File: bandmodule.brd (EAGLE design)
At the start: 100 x 80 mm, 15 parts

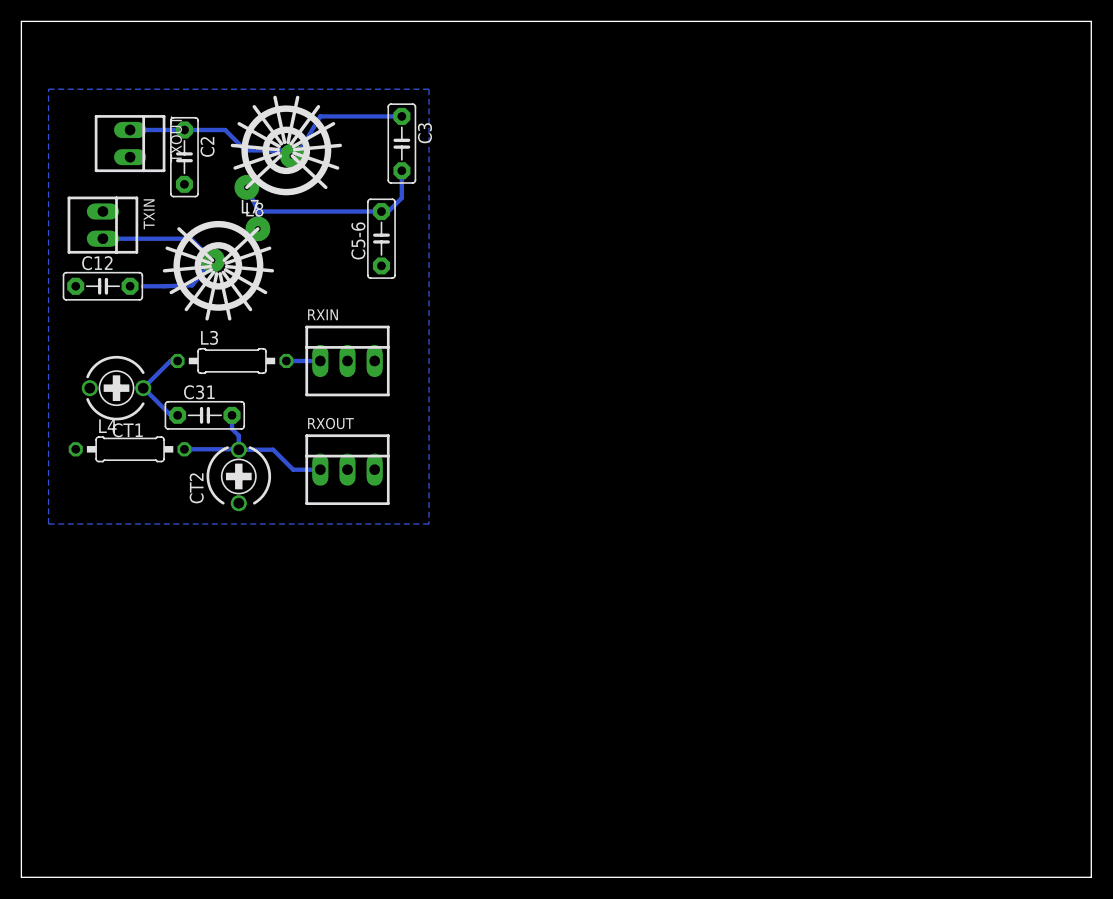
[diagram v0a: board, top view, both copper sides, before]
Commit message: Make board smaller
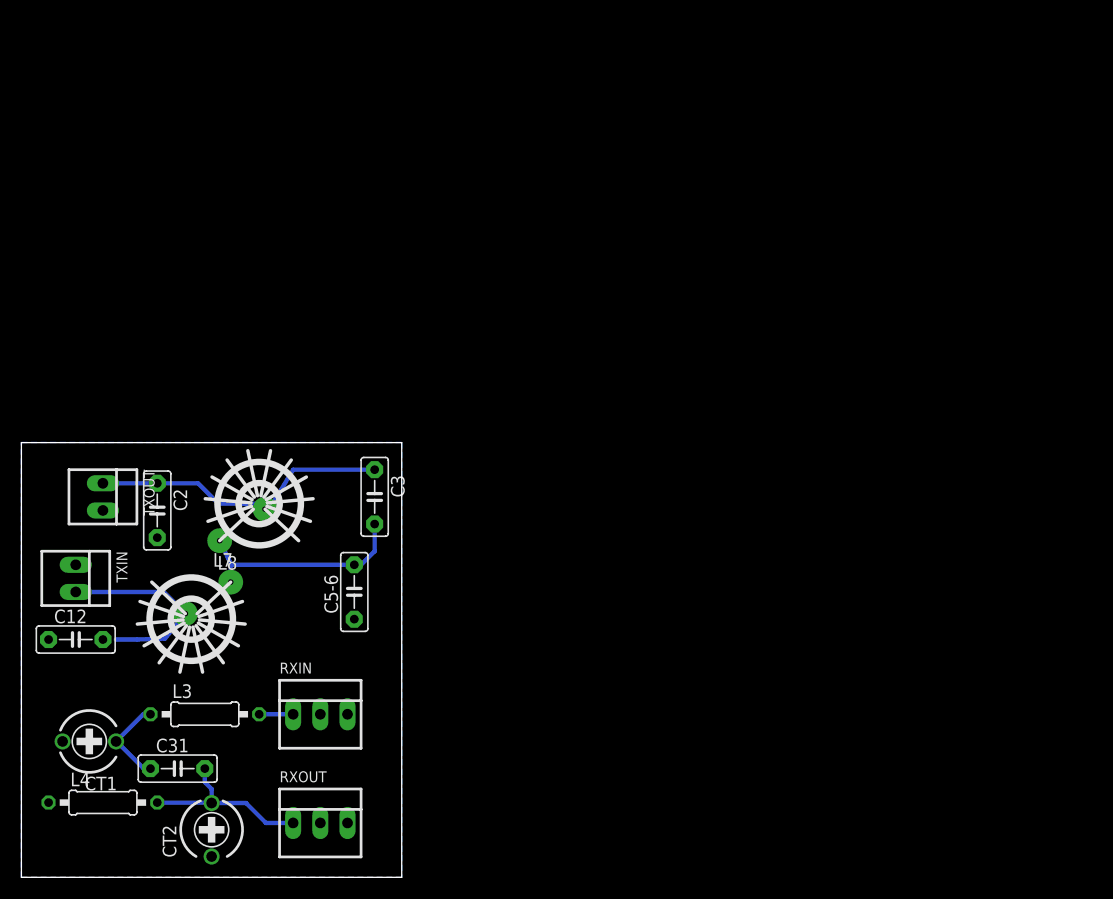
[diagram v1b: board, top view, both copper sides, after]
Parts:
- moved C2 33.1 mm to (12.7, 34.3)
- moved CT2 33.1 mm to (17.8, 4.45)
- moved L4 33.1 mm to (7.62, 6.99)
- moved RXOUT 33.1 mm to (27.9, 5.08)
- moved C12 33.1 mm to (5.08, 22.2)
- moved C3 33.1 mm to (33.0, 35.6)
- moved C31 33.1 mm to (14.6, 10.2)
- moved C5-6 33.1 mm to (31.1, 26.7)
- moved CT1 33.1 mm to (6.35, 12.7)
- moved L3 33.1 mm to (17.1, 15.2)
- moved L7 33.1 mm to (15.9, 24.1)
- moved L8 33.1 mm to (22.2, 34.9)
- moved RXIN 33.1 mm to (27.9, 15.2)
- moved TXIN 33.1 mm to (5.08, 27.9)
- moved TXOUT 33.1 mm to (7.62, 35.6)
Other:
- board size 100 x 80 mm -> 35.5 x 40.6 mm

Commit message: Readme, made more space for toroids
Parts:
- moved L7 1.42 mm to (17.1, 24.8)
- moved C3 1.14 mm to (32.1, 36.2)
- moved C5-6 1.14 mm to (30.2, 27.3)
- moved L8 0.71 mm to (21.9, 35.6), turned to 90 degrees
- moved C12 0.71 mm to (5.40, 22.9)
- moved CT1 0.64 mm to (6.35, 13.3)
- moved C31 0.63 mm to (14.6, 10.8)
- moved CT2 0.63 mm to (17.8, 5.08)
- moved L3 0.63 mm to (17.1, 15.9)
- moved L4 0.63 mm to (7.62, 7.62)
- moved RXIN 0.63 mm to (27.9, 15.9)
- moved RXOUT 0.63 mm to (27.9, 5.71)
- moved C2 0.63 mm to (12.7, 34.9)
- moved TXIN 0.63 mm to (5.08, 28.6)
- moved TXOUT 0.63 mm to (7.62, 36.2)
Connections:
- net GND: now also C12.1; no longer C12.2
- net N$6: now also C12.2; no longer C12.1
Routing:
- net N$8: track 33.7 -> 26.0 mm
- net N$5: track 20.7 -> 17.0 mm
- net N$6: track 18.7 -> 15.4 mm
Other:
- board size 35.5 x 40.6 mm -> 35.5 x 41.3 mm

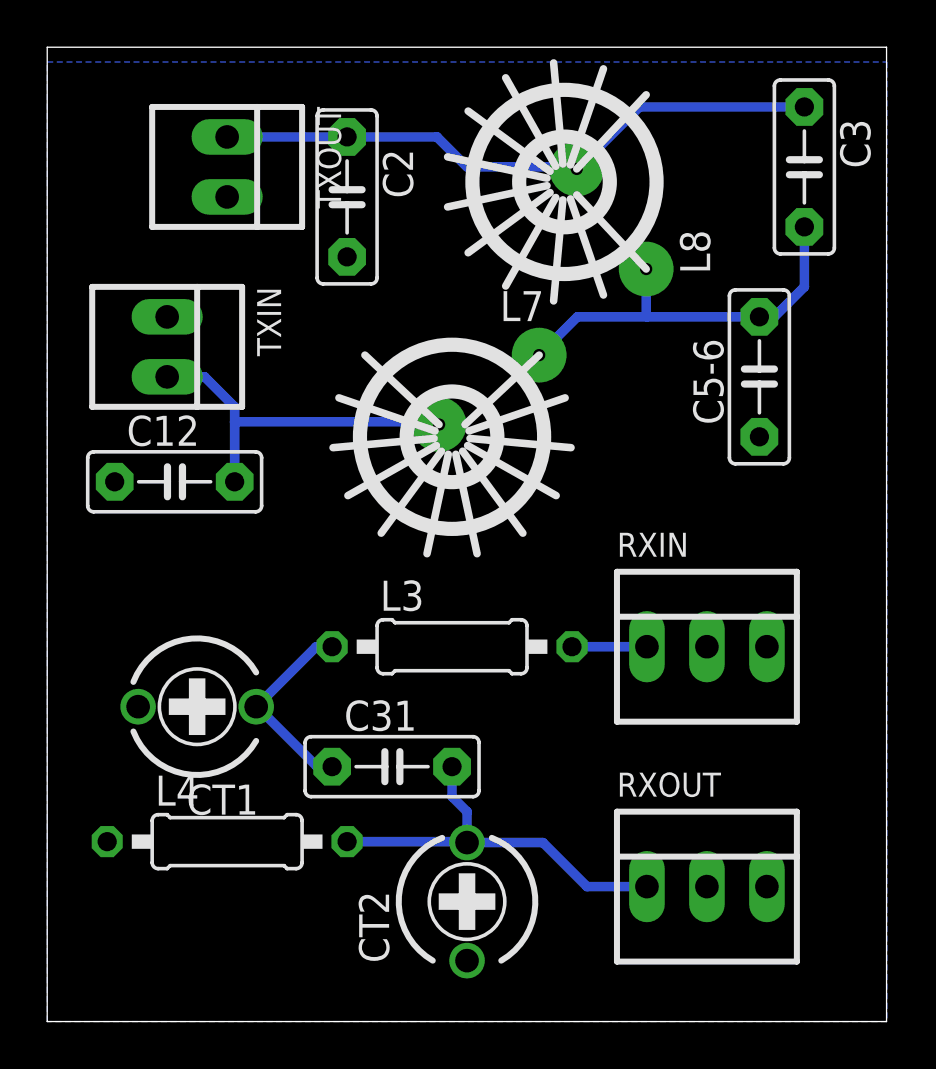
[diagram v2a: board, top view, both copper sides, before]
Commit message: Move labels, add white rectangle for band
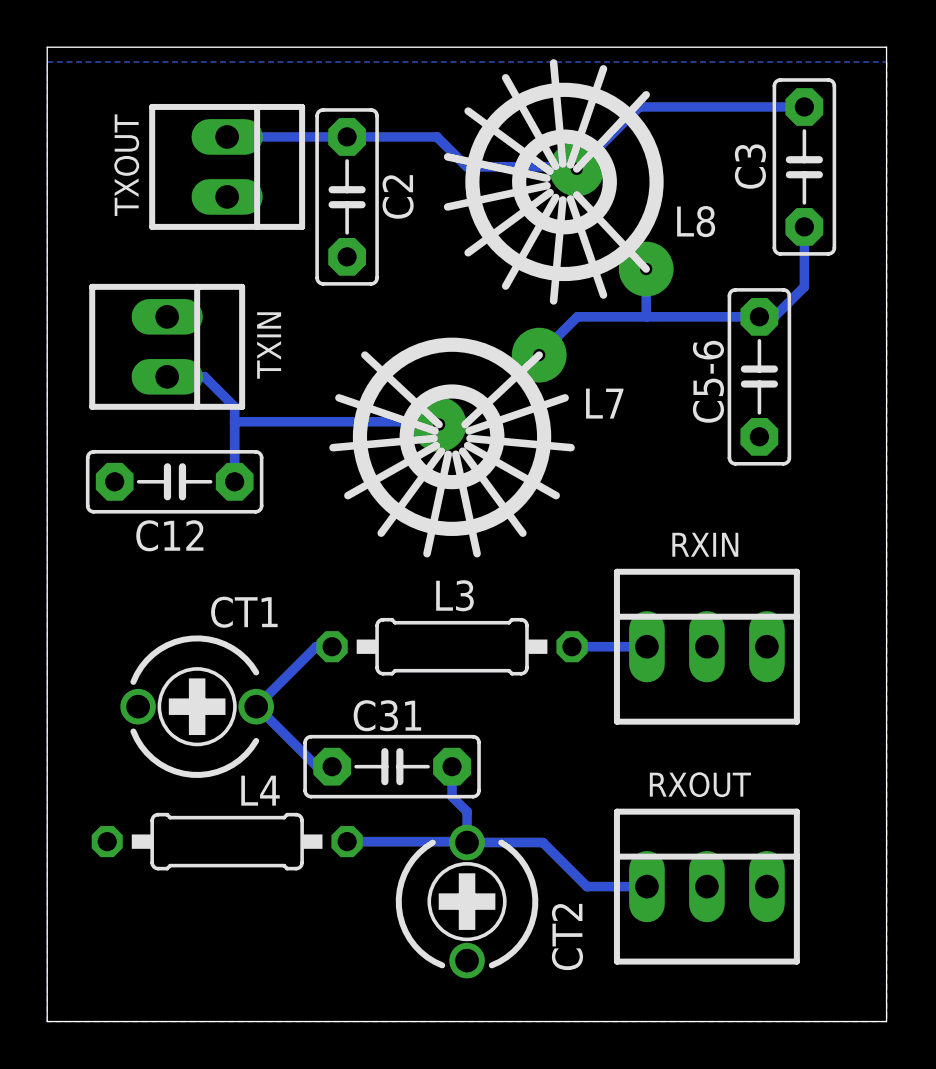
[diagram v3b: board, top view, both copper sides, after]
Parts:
- turned CT2 to 180 degrees
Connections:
- net GND: now also CT2.1; no longer CT2.2
- net N$4: now also CT2.2; no longer CT2.1
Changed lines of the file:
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@@
 <wire x1="35.5475" y1="41.265" x2="0" y2="41.265" width="0" layer="20"/>
 <wire x1="0" y1="41.265" x2="0" y2="0" width="0" layer="20"/>
+<rectangle x1="1.5875" y1="1.5875" x2="13.97" y2="6.0325" layer="51"/>
 </plain>
 <attributes>
@@
 </autorouter>
 <elements>
-<element name="C12" library="capacitor-wima" package="C5B2.5" value="150p" x="5.3975" y="22.86"/>
-<element name="C2" library="capacitor-wima" package="C5B2.5" value="150p" x="12.7" y="34.925" rot="R270"/>
-<element name="C3" library="capacitor-wima" package="C5B2.5" value="33p" x="32.0675" y="36.195" rot="R270"/>
-<element name="C31" library="capacitor-wima" package="C5B2.5" value="5p" x="14.605" y="10.795"/>
-<element name="C5-6" library="capacitor-wima" package="C5B2.5" value="330p" x="30.1625" y="27.305" rot="R90"/>
-<element name="CT1" library="rcl" package="CTRIMTZ03" value="60p" x="6.35" y="13.335" rot="R90"/>
-<element name="CT2" library="rcl" package="CTRIMTZ03" value="60p" x="17.78" y="5.08"/>
-<element name="L7" library="toroids" package="T30-2-28AWG-12T" value="T30-2 / 12T" x="17.145" y="24.765" rot="R180"/>
-<element name="L8" library="toroids" package="T30-2-28AWG-12T" value="T30-2 / 15T" x="21.9075" y="35.56" rot="R90"/>
-<element name="RXIN" library="con-molex" package="22-23-2031" value="22-23-2031" x="27.94" y="15.875">
+<element name="C12" library="capacitor-wima" package="C5B2.5" value="150p" x="5.3975" y="22.86" smashed="yes">
+<attribute name="NAME" x="3.683" y="19.939" size="1.27" layer="25" ratio="10"/>
+</element>
+<element name="C2" library="capacitor-wima" package="C5B2.5" value="150p" x="12.7" y="34.925" smashed="yes" rot="R270">
+<attribute name="NAME" x="14.224" y="36.0045" size="1.27" layer="25" ratio="10" rot="R270"/>
+</element>
+<element name="C3" library="capacitor-wima" package="C5B2.5" value="33p" x="32.0675" y="36.195" smashed="yes" rot="R270">
+<attribute name="NAME" x="29.1465" y="37.2745" size="1.27" layer="25" ratio="10" rot="R270"/>
+</element>
+<element name="C31" library="capacitor-wima" package="C5B2.5" value="5p" x="14.605" y="10.795" smashed="yes">
+<attribute name="NAME" x="12.8905" y="12.319" size="1.27" layer="25" ratio="10"/>
+</element>
+<element name="C5-6" library="capacitor-wima" package="C5B2.5" value="330p" x="30.1625" y="27.305" smashed="yes" rot="R90">
+<attribute name="NAME" x="28.6385" y="25.273" size="1.27" layer="25" ratio="10" rot="R90"/>
+</element>
+<element name="CT1" library="rcl" package="CTRIMTZ03" value="60p" x="6.35" y="13.335" smashed="yes" rot="R90">
+<attribute name="NAME" x="9.9025" y="17.9725" size="1.27" layer="25" rot="R180"/>
+</element>
+<element name="CT2" library="rcl" package="CTRIMTZ03" value="60p" x="17.78" y="5.08" smashed="yes" rot="R180">
+<attribute name="NAME" x="21.3975" y="5.14" size="1.27" layer="25" rot="R270"/>
+</element>
+<element name="L7" library="toroids" package="T30-2-28AWG-12T" value="T30-2 / 12T" x="17.145" y="24.765" smashed="yes" rot="R180">
+<attribute name="NAME" x="24.5375" y="26.8075" size="1.27" layer="25" rot="R180"/>
+</element>
+<element name="L8" library="toroids" package="T30-2-28AWG-12T" value="T30-2 / 15T" x="21.9075" y="35.56" smashed="yes" rot="R90">
+<attribute name="NAME" x="28.395" y="34.5175" size="1.27" layer="25" rot="R180"/>
+</element>
+<element name="RXIN" library="con-molex" package="22-23-2031" value="22-23-2031" x="27.94" y="15.875" smashed="yes">
 <attribute name="MF" value="MOLEX" x="27.94" y="15.875" size="1.778" layer="27" display="off"/>
 <attribute name="MPN" value="22-23-2031" x="27.94" y="15.875" size="1.778" layer="27" display="off"/>
+<attribute name="NAME" x="26.3525" y="19.685" size="1.016" layer="25" ratio="10"/>
 <attribute name="OC_FARNELL" value="1462950" x="27.94" y="15.875" size="1.778" layer="27" display="off"/>
 <attribute name="OC_NEWARK" value="30C0862" x="27.94" y="15.875" size="1.778" layer="27" display="off"/>
 </element>
-<element name="RXOUT" library="con-molex" package="22-23-2031" value="22-23-2031" x="27.94" y="5.715">
+<element name="RXOUT" library="con-molex" package="22-23-2031" value="22-23-2031" x="27.94" y="5.715" smashed="yes">
 <attribute name="MF" value="MOLEX" x="27.94" y="5.715" size="1.778" layer="27" display="off"/>
 <attribute name="MPN" value="22-23-2031" x="27.94" y="5.715" size="1.778" layer="27" display="off"/>
+<attribute name="NAME" x="25.4" y="9.525" size="1.016" layer="25" ratio="10"/>
 <attribute name="OC_FARNELL" value="1462950" x="27.94" y="5.715" size="1.778" layer="27" display="off"/>
 <attribute name="OC_NEWARK" value="30C0862" x="27.94" y="5.715" size="1.778" layer="27" display="off"/>
 </element>
-<element name="TXOUT" library="con-molex" package="22-23-2021" value="22-23-2021" x="7.62" y="36.195" rot="R270">
+<element name="TXOUT" library="con-molex" package="22-23-2021" value="22-23-2021" x="7.62" y="36.195" smashed="yes" rot="R270">
 <attribute name="MF" value="MOLEX" x="7.62" y="36.195" size="1.778" layer="27" rot="R270" display="off"/>
 <attribute name="MPN" value="22-23-2021" x="7.62" y="36.195" size="1.778" layer="27" rot="R270" display="off"/>
+<attribute name="NAME" x="2.8575" y="38.4175" size="1.016" layer="25" ratio="10" rot="R270"/>
 <attribute name="OC_FARNELL" value="1462926" x="7.62" y="36.195" size="1.778" layer="27" rot="R270" display="off"/>
 <attribute name="OC_NEWARK" value="25C3832" x="7.62" y="36.195" size="1.778" layer="27" rot="R270" display="off"/>
 </element>
-<element name="TXIN" library="con-molex" package="22-23-2021" value="22-23-2021" x="5.08" y="28.575" rot="R270">
+<element name="TXIN" library="con-molex" package="22-23-2021" value="22-23-2021" x="5.08" y="28.575" smashed="yes" rot="R270">
 <attribute name="MF" value="MOLEX" x="5.08" y="28.575" size="1.778" layer="27" rot="R270" display="off"/>
 <attribute name="MPN" value="22-23-2021" x="5.08" y="28.575" size="1.778" layer="27" rot="R270" display="off"/>
+<attribute name="NAME" x="8.89" y="30.1625" size="1.016" layer="25" ratio="10" rot="R270"/>
 <attribute name="OC_FARNELL" value="1462926" x="5.08" y="28.575" size="1.778" layer="27" rot="R270" display="off"/>
 <attribute name="OC_NEWARK" value="25C3832" x="5.08" y="28.575" size="1.778" layer="27" rot="R270" display="off"/>
 </element>
-<element name="L4" library="eagle-ltspice" package="0207/10" value="5.6uH" x="7.62" y="7.62">
+<element name="L4" library="eagle-ltspice" package="0207/10" value="5.6uH" x="7.62" y="7.62" smashed="yes">
+<attribute name="NAME" x="8.0645" y="9.144" size="1.27" layer="25" ratio="10"/>
 <attribute name="SPICEMODEL" value="NONE" x="7.62" y="7.62" size="1.778" layer="27" display="off"/>
 <attribute name="SPICEPREFIX" value="L" x="7.62" y="7.62" size="1.778" layer="27" display="off"/>
 </element>
-<element name="L3" library="eagle-ltspice" package="0207/10" value="5.6uH" x="17.145" y="15.875">
+<element name="L3" library="eagle-ltspice" package="0207/10" value="5.6uH" x="17.145" y="15.875" smashed="yes">
+<attribute name="NAME" x="16.3195" y="17.399" size="1.27" layer="25" ratio="10"/>
 <attribute name="SPICEMODEL" value="NONE" x="17.145" y="15.875" size="1.778" layer="27" display="off"/>
 <attribute name="SPICEPREFIX" value="L" x="17.145" y="15.875" size="1.778" layer="27" display="off"/>
@@
 <contactref element="RXOUT" pad="1"/>
 <contactref element="C31" pad="2"/>
-<contactref element="CT2" pad="1"/>
+<contactref element="CT2" pad="2"/>
 <contactref element="L4" pad="2"/>
 <wire x1="17.145" y1="10.795" x2="17.145" y2="9.525" width="0.4064" layer="16"/>
@@
 <contactref element="RXIN" pad="3"/>
 <contactref element="CT1" pad="1"/>
-<contactref element="CT2" pad="2"/>
+<contactref element="CT2" pad="1"/>
 <contactref element="C2" pad="2"/>
 <contactref element="C5-6" pad="1"/>

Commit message: Split up C5-6
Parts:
- added C6: unused, capacitor-wima:C5B2.5
- renumbered C5-6 to C5
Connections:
- net GND: now also C6.1
- net N$5: now also C6.2
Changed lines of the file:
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@@
 <attribute name="NAME" x="12.8905" y="12.319" size="1.27" layer="25" ratio="10"/>
 </element>
-<element name="C5-6" library="capacitor-wima" package="C5B2.5" value="330p" x="30.1625" y="27.305" smashed="yes" rot="R90">
-<attribute name="NAME" x="28.6385" y="25.273" size="1.27" layer="25" ratio="10" rot="R90"/>
+<element name="C5" library="capacitor-wima" package="C5B2.5" value="330p" x="30.1625" y="27.305" smashed="yes" rot="R90">
+<attribute name="NAME" x="33.0835" y="25.908" size="1.27" layer="25" ratio="10" rot="R90"/>
 </element>
 <element name="CT1" library="rcl" package="CTRIMTZ03" value="60p" x="6.35" y="13.335" smashed="yes" rot="R90">
@@
 </element>
 <element name="L7" library="toroids" package="T30-2-28AWG-12T" value="T30-2 / 12T" x="17.145" y="24.765" smashed="yes" rot="R180">
-<attribute name="NAME" x="24.5375" y="26.8075" size="1.27" layer="25" rot="R180"/>
+<attribute name="NAME" x="23.9025" y="23.6325" size="1.27" layer="25" rot="R180"/>
 </element>
 <element name="L8" library="toroids" package="T30-2-28AWG-12T" value="T30-2 / 15T" x="21.9075" y="35.56" smashed="yes" rot="R90">
@@
 <attribute name="SPICEPREFIX" value="L" x="17.145" y="15.875" size="1.778" layer="27" display="off"/>
 </element>
+<element name="C6" library="capacitor-wima" package="C5B2.5" value="unused" x="27.305" y="27.305" smashed="yes" rot="R90">
+<attribute name="NAME" x="25.781" y="25.908" size="1.27" layer="25" ratio="10" rot="R90"/>
+</element>
 </elements>
 <signals>
@@
 <contactref element="CT2" pad="1"/>
 <contactref element="C2" pad="2"/>
-<contactref element="C5-6" pad="1"/>
+<contactref element="C5" pad="1"/>
 <contactref element="C12" pad="1"/>
 <contactref element="L4" pad="1"/>
@@
 <vertex x="0" y="0"/>
 </polygon>
+<contactref element="C6" pad="1"/>
 </signal>
 <signal name="N$1">
@@
 <contactref element="L8" pad="P$2"/>
 <contactref element="L7" pad="P$2"/>
-<contactref element="C5-6" pad="2"/>
+<contactref element="C5" pad="2"/>
 <contactref element="C3" pad="2"/>
 <wire x1="30.1625" y1="29.845" x2="30.7975" y2="29.845" width="0.4064" layer="16"/>
 <wire x1="30.7975" y1="29.845" x2="32.0675" y2="31.115" width="0.4064" layer="16"/>
 <wire x1="32.0675" y1="31.115" x2="32.0675" y2="33.655" width="0.4064" layer="16"/>
-<wire x1="30.1625" y1="29.845" x2="25.4" y2="29.845" width="0.4064" layer="16"/>
 <wire x1="25.3675" y1="31.87" x2="25.3675" y2="29.8775" width="0.4064" layer="16"/>
 <wire x1="25.3675" y1="29.8775" x2="25.4" y2="29.845" width="0.4064" layer="16"/>
 <wire x1="25.4" y1="29.845" x2="22.455" y2="29.845" width="0.4064" layer="16"/>
 <wire x1="22.455" y1="29.845" x2="20.835" y2="28.225" width="0.4064" layer="16"/>
+<contactref element="C6" pad="2"/>
+<wire x1="25.3675" y1="29.8775" x2="27.305" y2="29.8775" width="0.4064" layer="16"/>
+<wire x1="27.305" y1="29.8775" x2="27.305" y2="29.845" width="0.4064" layer="16"/>
+<wire x1="27.305" y1="29.845" x2="30.1625" y2="29.845" width="0.4064" layer="16"/>
 </signal>
 <signal name="N$6">
